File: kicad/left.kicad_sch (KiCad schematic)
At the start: 101 parts, among them Q1 PMF170XP,115, Q2 FS8205A_C2830320, SW1 TS-1088-AR02016, U1 SN74LVC1G17DBVR, U2 E73-2G4M08S1C, U3 SN74LVC1G74DQER, U4 S2B-PH-K-S(LF)(SN), U5 BL8573CS8TR, U6 DW01A_C42380662, U7 LP5024RSMR, U8 MAX17048, X1 FC-13532.768KHZ9PF20PPM

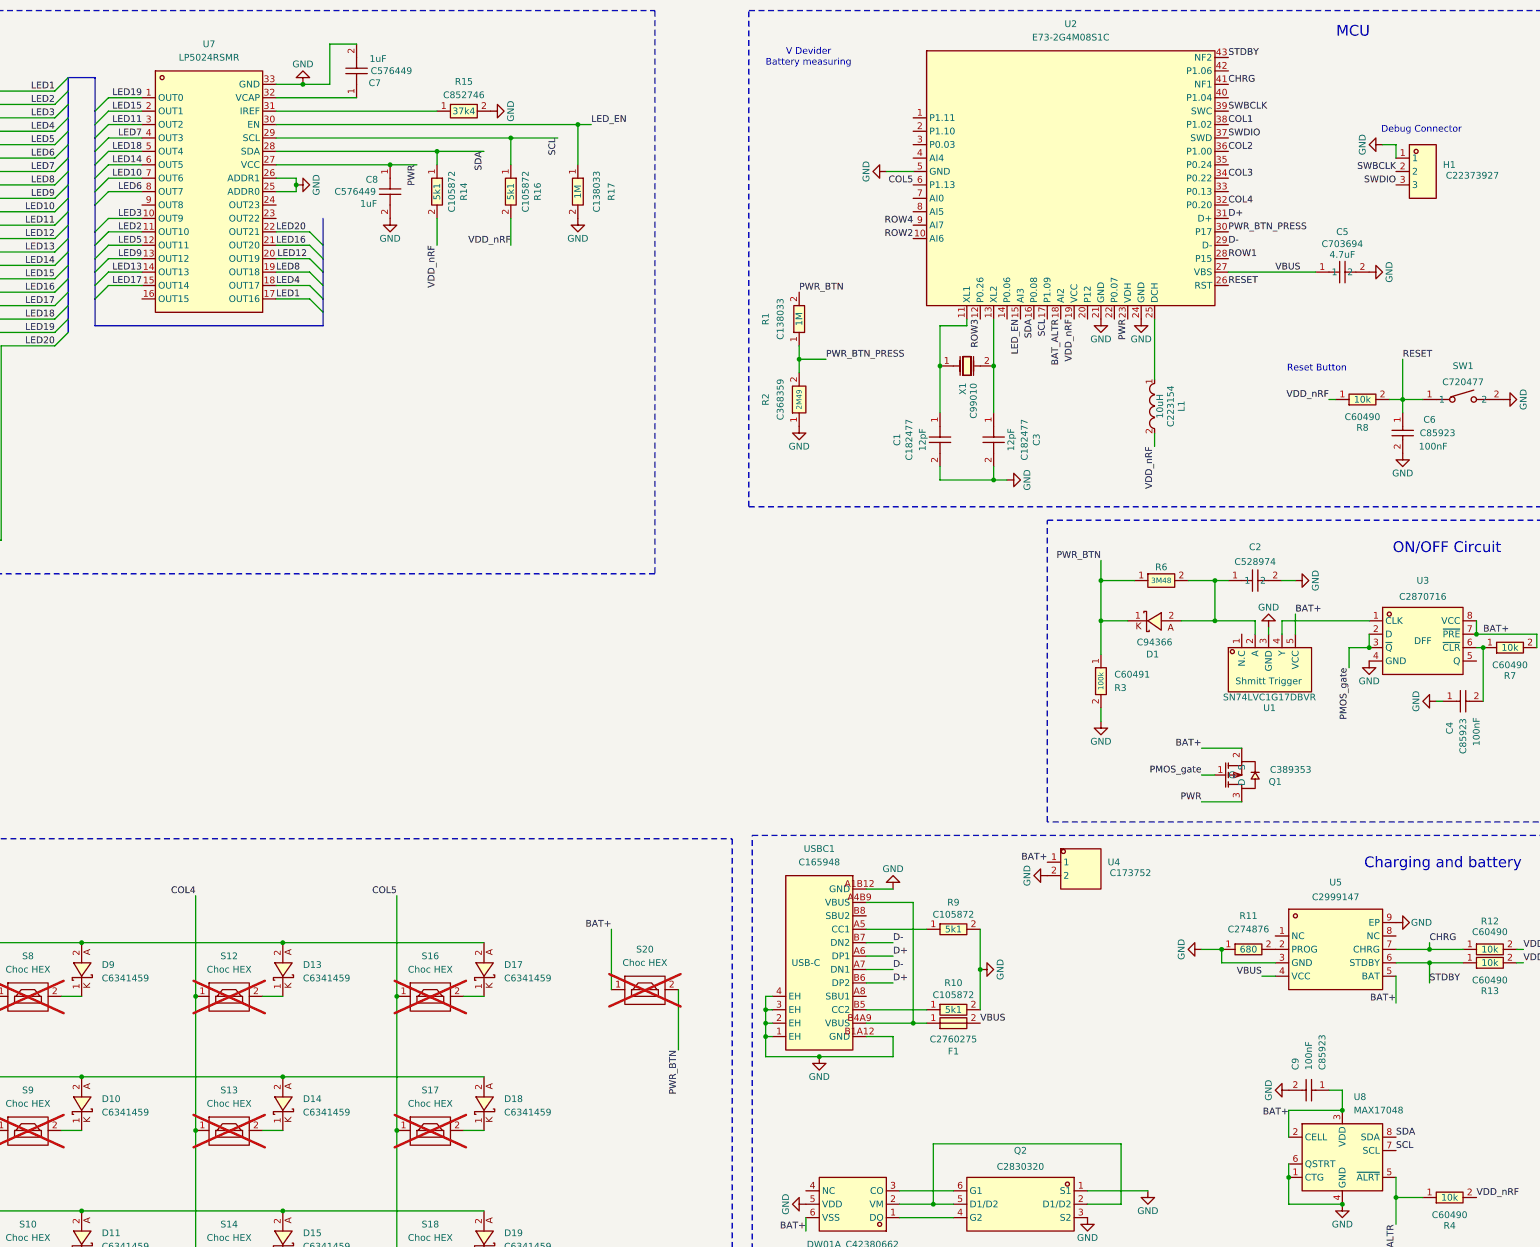
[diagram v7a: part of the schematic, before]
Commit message: finished. needes inspection. added battery measurer. wired left side
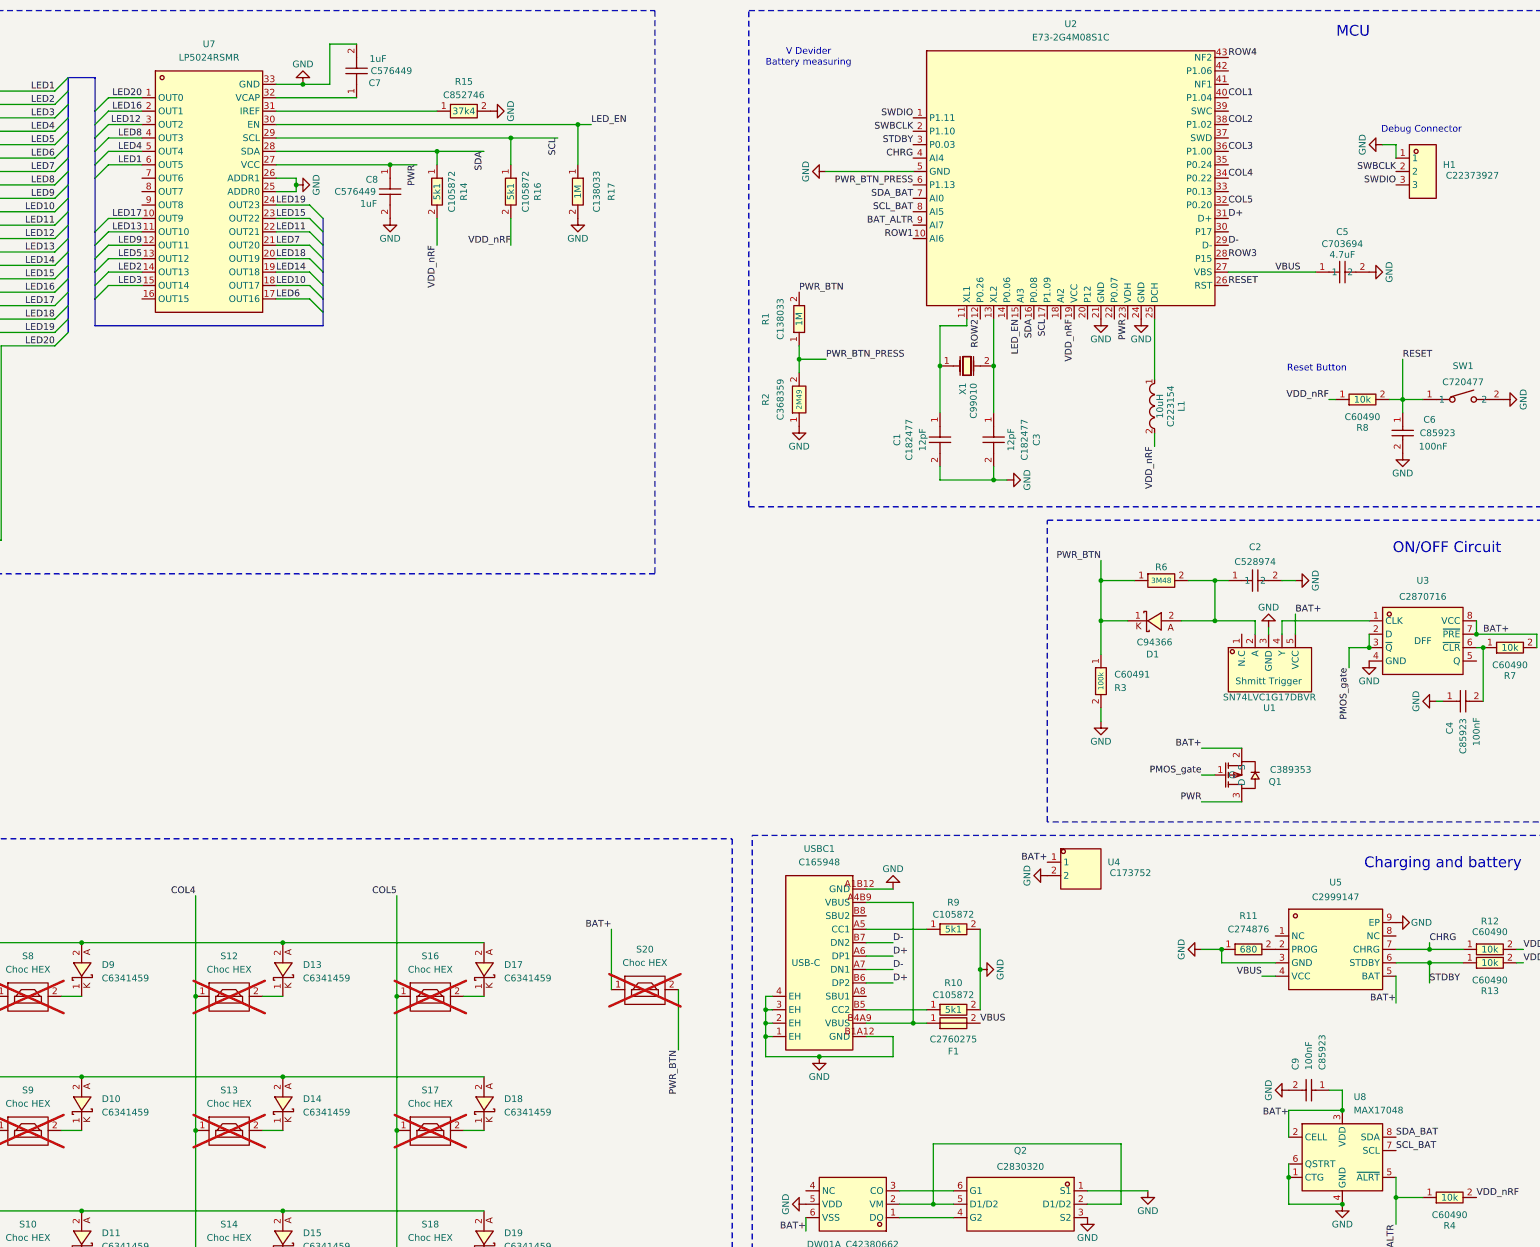
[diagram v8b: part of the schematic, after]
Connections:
- net BAT_ALTR: now also U2.9 (AI7); no longer U2.18 (AI2)
- net CHRG: now also U2.4 (AI4); no longer U2.41 (NF1)
- net COL1: now also U2.40 (P1.04); no longer U2.38 (P1.02)
- net COL2: now also U2.38 (P1.02); no longer U2.36 (P1.00)
- net COL3: now also U2.36 (P1.00); no longer U2.34 (P0.22)
- net COL4: now also U2.34 (P0.22); no longer U2.32 (P0.20)
- net COL5: now also U2.32 (P0.20); no longer U2.6 (P1.13)
- net LED1: now also U7.6 (OUT5); no longer U7.17 (OUT16)
- net LED10: now also U7.18 (OUT17); no longer U7.7 (OUT6)
- net LED11: now also U7.22 (OUT21); no longer U7.3 (OUT2)
- net LED12: now also U7.3 (OUT2); no longer U7.20 (OUT19)
- net LED13: now also U7.11 (OUT10); no longer U7.14 (OUT13)
- net LED14: now also U7.19 (OUT18); no longer U7.6 (OUT5)
- net LED15: now also U7.23 (OUT22); no longer U7.2 (OUT1)
- net LED16: now also U7.2 (OUT1); no longer U7.21 (OUT20)
- net LED17: now also U7.10 (OUT9); no longer U7.15 (OUT14)
- net LED18: now also U7.20 (OUT19); no longer U7.5 (OUT4)
- net LED19: now also U7.24 (OUT23); no longer U7.1 (OUT0)
- net LED2: now also U7.14 (OUT13); no longer U7.11 (OUT10)
- net LED20: now also U7.1 (OUT0); no longer U7.22 (OUT21)
- net LED3: now also U7.15 (OUT14); no longer U7.10 (OUT9)
- net LED4: now also U7.5 (OUT4); no longer U7.18 (OUT17)
- net LED5: now also U7.13 (OUT12); no longer U7.12 (OUT11)
- net LED6: now also U7.17 (OUT16); no longer U7.8 (OUT7)
- net LED7: now also U7.21 (OUT20); no longer U7.4 (OUT3)
- net LED8: now also U7.4 (OUT3); no longer U7.19 (OUT18)
- net LED9: now also U7.12 (OUT11); no longer U7.13 (OUT12)
- net PWR_BTN_PRESS: now also U2.6 (P1.13); no longer U2.30 (P17)
- net ROW1: now also U2.10 (AI6); no longer U2.28 (P15)
- net ROW2: now also U2.12 (P0.26); no longer U2.10 (AI6)
- net ROW3: now also U2.28 (P15); no longer U2.12 (P0.26)
- net ROW4: now also U2.43 (NF2); no longer U2.9 (AI7)
- net SCL: no longer U8.7 (SCL)
- net SDA: no longer U8.8 (SDA)
- net STDBY: now also U2.3 (P0.03); no longer U2.43 (NF2)
- net SWBCLK: now also U2.2 (P1.10); no longer U2.39 (SWC)
- net SWDIO: now also U2.1 (P1.11); no longer U2.37 (SWD)
- net SDA_BAT: now reaches U2.7 (AI0)
- net SDA_BAT: now also U8.8 (SDA)
- net SCL_BAT: now reaches U2.8 (AI5)
- net SCL_BAT: now also U8.7 (SCL)
